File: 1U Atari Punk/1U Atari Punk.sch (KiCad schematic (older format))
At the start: 17 parts

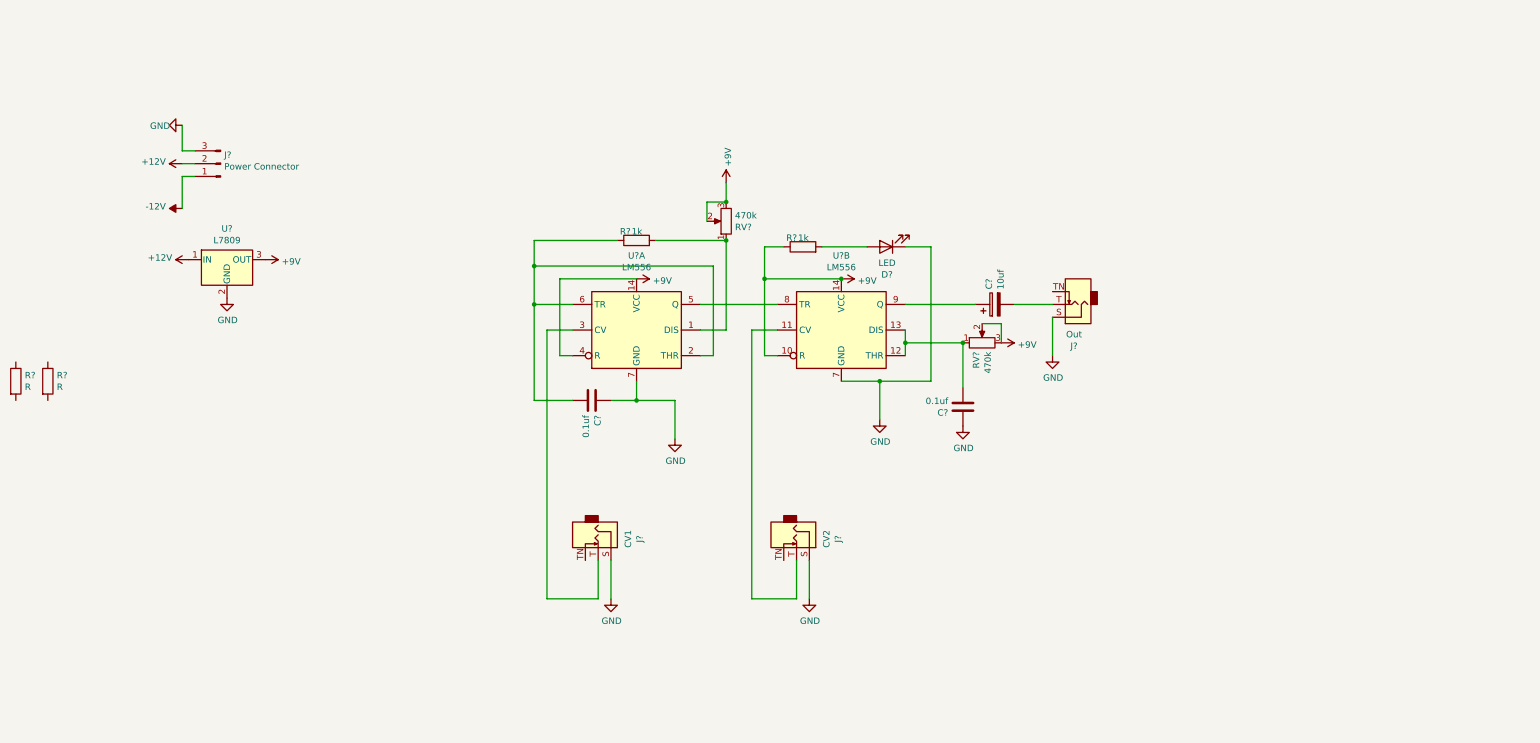
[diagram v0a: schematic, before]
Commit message: Cleaned up the schematic
I copied the components and made a cleaned up version for comparison. Make sure to delete the original before continuing
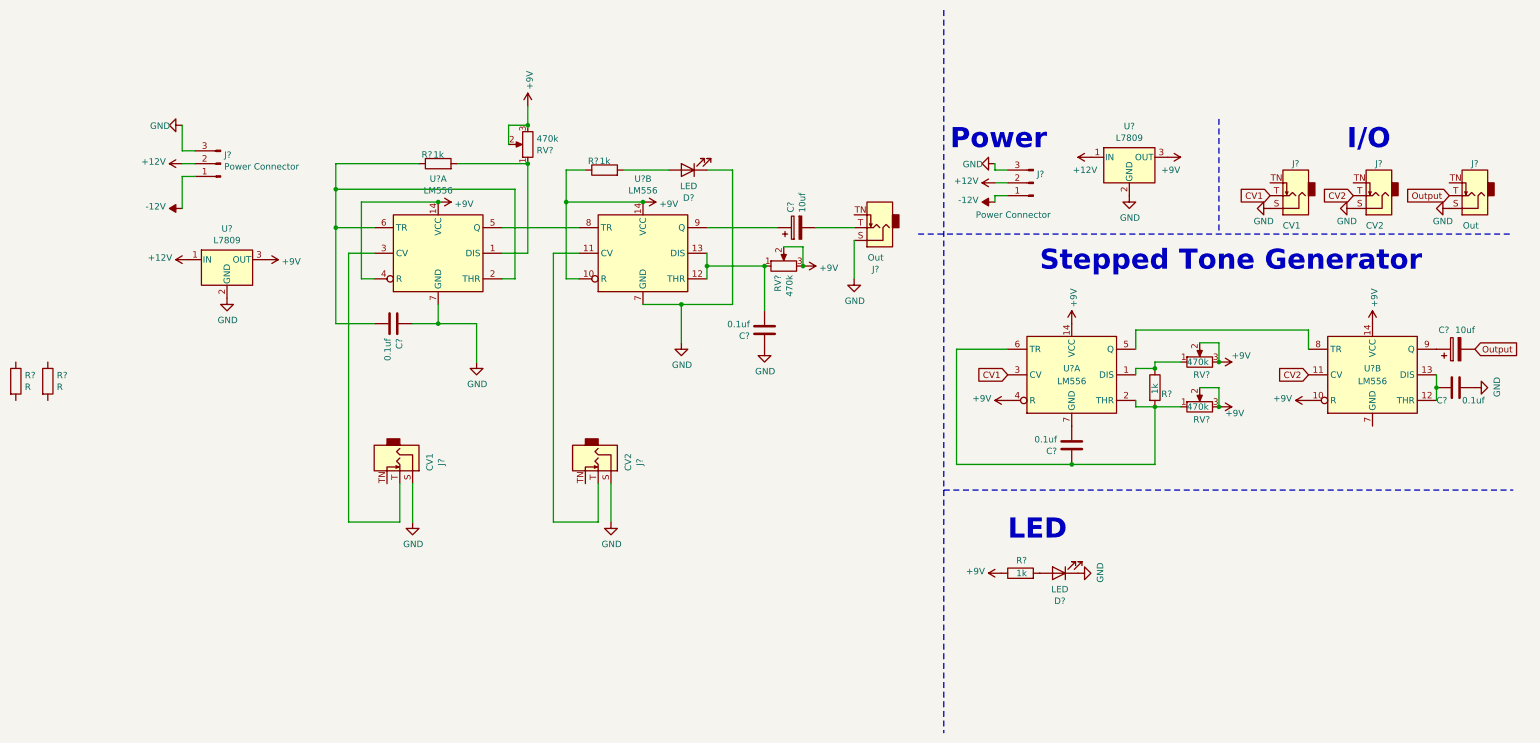
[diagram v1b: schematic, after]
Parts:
- added C? (x2): 0.1uf, symbol Device:C
- added C?: 10uf, symbol Device:CP
- added D?: LED, symbol Device:LED
- added J?: CV1, symbol Connector:AudioJack2_SwitchT
- added J?: CV2, symbol Connector:AudioJack2_SwitchT
- added J?: Out, symbol Connector:AudioJack2_SwitchT
- added J?: Power Connector, symbol Connector:Conn_01x03_Male
- added R? (x2): 1k, symbol Device:R
- added RV? (x2): 470k, symbol Device:R_POT
- added U? (x2): LM556, symbol Timer:LM556
- added U?: L7809, symbol Regulator_Linear:L7809
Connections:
- net +12V: now also J?.2 (Pin_2), U?.1 (IN)
- net +9V: now also R?.1, RV?.2, RV?.2, RV?.3, RV?.3, U?.10 (R), U?.14 (VCC), U?.14 (VCC), U?.3 (OUT), U?.4 (R)
- net -12V: now also J?.1 (Pin_1)
- net GND: now also C?.1, D?.1 (K), J?.3 (Pin_3), J?.S, J?.S, J?.S, U?.2 (GND)
- new net: C?.1, R?.2, RV?.1, U?.2 (THR), U?.6 (TR)
- new net: C?.2, U?.12 (THR), U?.13 (DIS)
- new net: D?.2 (A), R?.2
- new net: C?.1, U?.9 (Q)
- new net: R?.1, RV?.1, U?.1 (DIS)
- new net: U?.5 (Q), U?.8 (TR)
- new net: C?.2, U?.7 (GND)
- new net CV1: J?.T, U?.3 (CV)
- new net CV2: J?.T, U?.11 (CV)
- new net Output: C?.2, J?.T
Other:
- note added: "I/O"
- note added: "LED"
- note added: "Power\n"
- note added: "Stepped Tone Generator"
- moved on the sheet: C?, D?, J?, R?, RV?, U?A, U?B

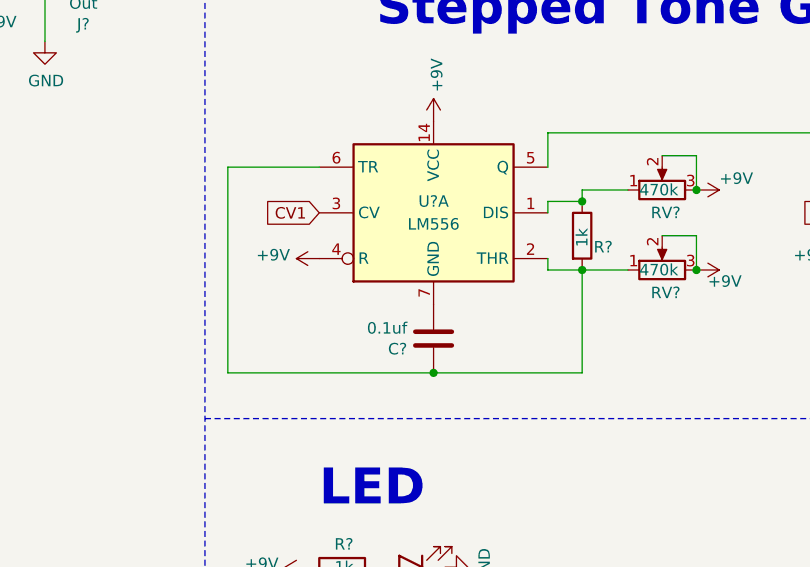
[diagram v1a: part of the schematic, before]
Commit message: Fixed Ground on pin 7
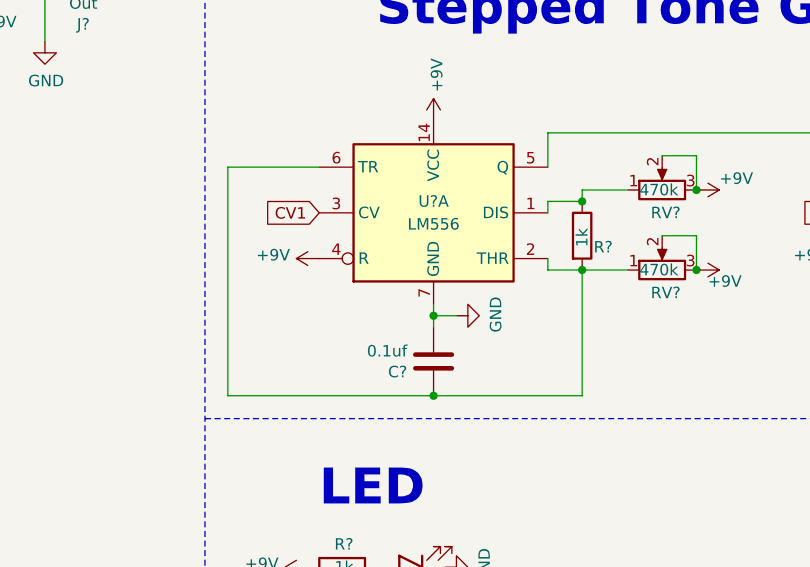
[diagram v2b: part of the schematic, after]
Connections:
- net GND: now also C?.2, U?.7 (GND)
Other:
- moved on the sheet: C?
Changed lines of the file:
@@
 L Device:C C?
 U 1 1 5F63280D
-P 7750 3100
-F 0 "C?" H 7865 3146 50  0000 L CNN
-F 1 "0.1uf" H 7865 3055 50  0000 L CNN
-F 2 "" H 7788 2950 50  0001 C CNN
-F 3 "~" H 7750 3100 50  0001 C CNN
-	1    7750 3100
+P 7750 3200
+F 0 "C?" H 7865 3246 50  0000 L CNN
+F 1 "0.1uf" H 7865 3155 50  0000 L CNN
+F 2 "" H 7788 3050 50  0001 C CNN
+F 3 "~" H 7750 3200 50  0001 C CNN
+	1    7750 3200
 	-1   0    0    1
 $EndComp
@@
 Connection ~ 8900 2800
 Wire Wire Line
-	8400 3250 7750 3250
-Wire Wire Line
-	7750 3250 6850 3250
-Wire Wire Line
-	6850 3250 6850 2350
+	8400 3350 7750 3350
+Wire Wire Line
+	7750 3350 6850 3350
 Wire Wire Line
 	6850 2350 7250 2350
-Connection ~ 7750 3250
+Connection ~ 7750 3350
 $Comp
 L power:+9V #PWR?
@@
 	8250 2200 9600 2200
 Wire Wire Line
-	8400 2800 8400 3250
-Wire Wire Line
 	8400 2450 8600 2450
 Wire Wire Line
@@
 Wire Notes Line
 	6750 3450 11200 3450
+Wire Wire Line
+	8400 2800 8400 3350
+Wire Wire Line
+	7750 3050 7750 3000
+Wire Wire Line
+	6850 2350 6850 3350
+$Comp
+L power:GND #PWR?
+U 1 1 5F640AC9
+P 7850 3000
+F 0 "#PWR?" H 7850 2750 50  0001 C CNN
+F 1 "GND" H 7855 2827 50  0000 C CNN
+F 2 "" H 7850 3000 50  0001 C CNN
+F 3 "" H 7850 3000 50  0001 C CNN
+	1    7850 3000
+	0    -1   -1   0
+$EndComp
+Wire Wire Line
+	7850 3000 7750 3000
+Connection ~ 7750 3000
+Wire Wire Line
+	7750 3000 7750 2950
 $EndSCHEMATC

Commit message: Started the big logic module
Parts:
- C?: value 0.1uf -> 0.01uf
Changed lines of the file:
@@
 P 7750 3200
 F 0 "C?" H 7865 3246 50  0000 L CNN
-F 1 "0.1uf" H 7865 3155 50  0000 L CNN
+F 1 "0.01uf" H 7865 3155 50  0000 L CNN
 F 2 "" H 7788 3050 50  0001 C CNN
 F 3 "~" H 7750 3200 50  0001 C CNN
